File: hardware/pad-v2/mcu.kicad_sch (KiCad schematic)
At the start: 11 parts, among them J201 TYPE-C-31-M-12, SW201 SW_Push, SW202 SW_Push, U201 ESP32-S3-MINI-1-N8, U202 TPD4E1U06DBVR

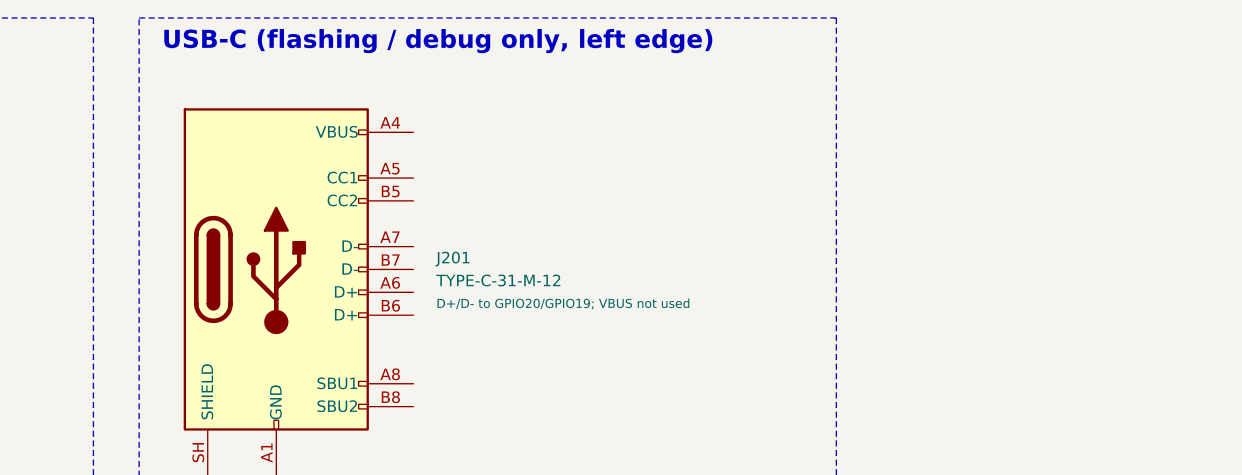
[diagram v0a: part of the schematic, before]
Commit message: Pad v2: GPIO map for routing, PAD_WIRING.md (component-by-component), connection model + checker; battery 2-pin + NTC header, USB-C to the front edge, LED chain starts at key 9
Co-Authored-By: Claude Opus 5.5 <noreply@anthropic.com>
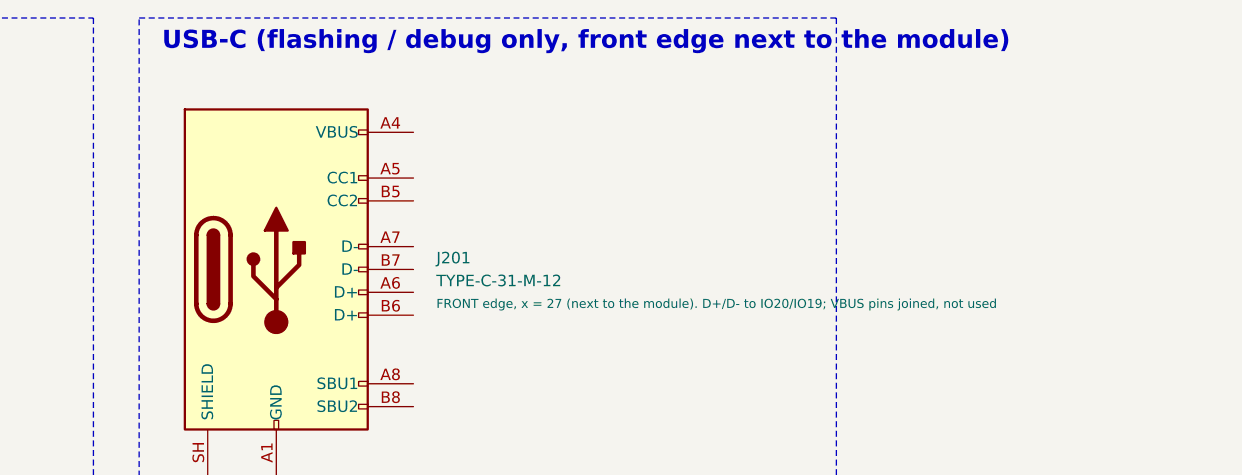
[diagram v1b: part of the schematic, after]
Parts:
- J201: Note D+/D- to GPIO20/GPIO19; VBUS not used -> FRONT edge, x = 27 (next to the module). D+/D- to IO20/IO19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
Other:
- note added: "USB-C (flashing / debug only, front edge next to the module)"
- note removed: "USB-C (flashing / debug only, left edge)"
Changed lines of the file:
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@@
 		)
 	)
-	(text "USB-C (flashing / debug only, left edge)"
+	(text "USB-C (flashing / debug only, front edge next to the module)"
 		(exclude_from_sim no)
 		(at 171.45 21.59 0)
@@
 		(instances
 			(project "pad-v2"
-				(path "/c348787c-35a6-4c40-81d7-0eeb948bfe4d/24fc9cbe-c5a7-4a31-aa16-34ec958d99a1"
+				(path "/aa63e03b-1ac8-4926-b623-c7b31956768e/70237507-d4af-4628-8cf6-83ee1d44b238"
 					(reference "U201")
 					(unit 1)
@@
 		(instances
 			(project "pad-v2"
-				(path "/c348787c-35a6-4c40-81d7-0eeb948bfe4d/24fc9cbe-c5a7-4a31-aa16-34ec958d99a1"
+				(path "/aa63e03b-1ac8-4926-b623-c7b31956768e/70237507-d4af-4628-8cf6-83ee1d44b238"
 					(reference "C201")
 					(unit 1)
@@
 		(instances
 			(project "pad-v2"
-				(path "/c348787c-35a6-4c40-81d7-0eeb948bfe4d/24fc9cbe-c5a7-4a31-aa16-34ec958d99a1"
+				(path "/aa63e03b-1ac8-4926-b623-c7b31956768e/70237507-d4af-4628-8cf6-83ee1d44b238"
 					(reference "C202")
 					(unit 1)
@@
 		(instances
 			(project "pad-v2"
-				(path "/c348787c-35a6-4c40-81d7-0eeb948bfe4d/24fc9cbe-c5a7-4a31-aa16-34ec958d99a1"
+				(path "/aa63e03b-1ac8-4926-b623-c7b31956768e/70237507-d4af-4628-8cf6-83ee1d44b238"
 					(reference "R201")
 					(unit 1)
@@
 		(instances
 			(project "pad-v2"
-				(path "/c348787c-35a6-4c40-81d7-0eeb948bfe4d/24fc9cbe-c5a7-4a31-aa16-34ec958d99a1"
+				(path "/aa63e03b-1ac8-4926-b623-c7b31956768e/70237507-d4af-4628-8cf6-83ee1d44b238"
 					(reference "C203")
 					(unit 1)
@@
 		(instances
 			(project "pad-v2"
-				(path "/c348787c-35a6-4c40-81d7-0eeb948bfe4d/24fc9cbe-c5a7-4a31-aa16-34ec958d99a1"
+				(path "/aa63e03b-1ac8-4926-b623-c7b31956768e/70237507-d4af-4628-8cf6-83ee1d44b238"
 					(reference "SW201")
 					(unit 1)
@@
 		(instances
 			(project "pad-v2"
-				(path "/c348787c-35a6-4c40-81d7-0eeb948bfe4d/24fc9cbe-c5a7-4a31-aa16-34ec958d99a1"
+				(path "/aa63e03b-1ac8-4926-b623-c7b31956768e/70237507-d4af-4628-8cf6-83ee1d44b238"
 					(reference "SW202")
 					(unit 1)
@@
 			)
 		)
-		(property "Note" "D+/D- to GPIO20/GPIO19; VBUS not used"
+		(property "Note" "FRONT edge, x = 27 (next to the module). D+/D- to IO20/IO19; VBUS pins joined, not used"
 			(at 201.93 49.53 0)
 			(show_name no)
@@
 		(instances
 			(project "pad-v2"
-				(path "/c348787c-35a6-4c40-81d7-0eeb948bfe4d/24fc9cbe-c5a7-4a31-aa16-34ec958d99a1"
+				(path "/aa63e03b-1ac8-4926-b623-c7b31956768e/70237507-d4af-4628-8cf6-83ee1d44b238"
 					(reference "J201")
 					(unit 1)
@@
 		(instances
 			(project "pad-v2"
-				(path "/c348787c-35a6-4c40-81d7-0eeb948bfe4d/24fc9cbe-c5a7-4a31-aa16-34ec958d99a1"
+				(path "/aa63e03b-1ac8-4926-b623-c7b31956768e/70237507-d4af-4628-8cf6-83ee1d44b238"
 					(reference "U202")
 					(unit 1)
@@
 		(instances
 			(project "pad-v2"
-				(path "/c348787c-35a6-4c40-81d7-0eeb948bfe4d/24fc9cbe-c5a7-4a31-aa16-34ec958d99a1"
+				(path "/aa63e03b-1ac8-4926-b623-c7b31956768e/70237507-d4af-4628-8cf6-83ee1d44b238"
 					(reference "R202")
 					(unit 1)
@@
 		(instances
 			(project "pad-v2"
-				(path "/c348787c-35a6-4c40-81d7-0eeb948bfe4d/24fc9cbe-c5a7-4a31-aa16-34ec958d99a1"
+				(path "/aa63e03b-1ac8-4926-b623-c7b31956768e/70237507-d4af-4628-8cf6-83ee1d44b238"
 					(reference "R203")
 					(unit 1)
